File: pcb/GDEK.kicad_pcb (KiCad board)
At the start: 2 copper layers, 133 x 103.5 mm, 101 parts, among them J1 TYPE-C-31-M-13C, J2 AudioJack4, SW1 SK6812MINI, SW10 SK6812MINI, SW11 SK6812MINI, SW12 SK6812MINI, SW13 SK6812MINI, SW14 SK6812MINI, SW15 SK6812MINI, SW16 SK6812MINI, SW17 SK6812MINI, SW18 SK6812MINI, SW19 SK6812MINI, SW2 SK6812MINI, SW20 SK6812MINI, SW21 SK6812MINI, SW22 SK6812MINI, SW23 SK6812MINI, SW24 SK6812MINI, SW25 SK6812MINI, SW26 SK6812MINI, SW27 SK6812MINI, SW28 SK6812MINI, SW29 SK6812MINI, SW3 SK6812MINI, SW30 SK6812MINI, SW31 RotaryEncoder_Switch, SW4 SK6812MINI, SW5 SK6812MINI, SW6 SK6812MINI, SW7 SK6812MINI, SW8 SK6812MINI, SW9 SK6812MINI, U1 RP2040, U2 W25Q128JVS, U3 74AHCT1G125, U4 USBLC6-2P6, U5 XC6210B332MR, Y1 ABM8-272-T3

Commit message: ♻️ Replace LED and reroute them
They are flipped on odd rows to have a better layout not requiring any layer switch because of the new LED footprint with mouse ears.
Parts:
- added C17: 100nF, Capacitor_SMD:C_0402_1005Metric, B.Cu at (137.5, 43.5)
- added C18: 100nF, Capacitor_SMD:C_0402_1005Metric, B.Cu at (24.2, 43.8)
- added C19: 100nF, Capacitor_SMD:C_0402_1005Metric, B.Cu at (-6.95, 22.3)
- added C20: 100nF, Capacitor_SMD:C_0402_1005Metric, B.Cu at (-6.95, 24.3)
- added C21: 100nF, Capacitor_SMD:C_0402_1005Metric, B.Cu at (-6.95, 26.2)
- added C22: 100nF, Capacitor_SMD:C_0402_1005Metric, B.Cu at (-6.95, 28.2)
- added C23: 100nF, Capacitor_SMD:C_0402_1005Metric, B.Cu at (-6.95, 30.2)
- added C24: 100nF, Capacitor_SMD:C_0402_1005Metric, B.Cu at (-6.95, 32.2)
- added C25: 100nF, Capacitor_SMD:C_0402_1005Metric, B.Cu at (-6.95, 34.1)
- added C26: 100nF, Capacitor_SMD:C_0402_1005Metric, B.Cu at (-6.95, 36.1)
- added C27: 100nF, Capacitor_SMD:C_0402_1005Metric, B.Cu at (-6.95, 38.1)
- added C28: 100nF, Capacitor_SMD:C_0402_1005Metric, B.Cu at (-6.95, 40.0)
- added C29: 100nF, Capacitor_SMD:C_0402_1005Metric, B.Cu at (-6.95, 42.0)
- added C30: 100nF, Capacitor_SMD:C_0402_1005Metric, B.Cu at (-9.82, 22.3)
- added C31: 100nF, Capacitor_SMD:C_0402_1005Metric, B.Cu at (-9.82, 24.3)
- added C32: 100nF, Capacitor_SMD:C_0402_1005Metric, B.Cu at (-9.82, 26.2)
- added C33: 100nF, Capacitor_SMD:C_0402_1005Metric, B.Cu at (-9.82, 28.2)
- added C34: 100nF, Capacitor_SMD:C_0402_1005Metric, B.Cu at (-9.82, 30.2)
- added C35: 100nF, Capacitor_SMD:C_0402_1005Metric, B.Cu at (-9.82, 32.2)
- added C36: 100nF, Capacitor_SMD:C_0402_1005Metric, B.Cu at (-9.82, 34.1)
- added C37: 100nF, Capacitor_SMD:C_0402_1005Metric, B.Cu at (-9.82, 36.1)
- added C38: 100nF, Capacitor_SMD:C_0402_1005Metric, B.Cu at (-9.82, 38.1)
- added C39: 100nF, Capacitor_SMD:C_0402_1005Metric, B.Cu at (-9.82, 40.0)
- added C40: 100nF, Capacitor_SMD:C_0402_1005Metric, B.Cu at (-9.82, 42.0)
- added C41: 100nF, Capacitor_SMD:C_0402_1005Metric, B.Cu at (-12.7, 22.3)
- added C42: 100nF, Capacitor_SMD:C_0402_1005Metric, B.Cu at (-12.7, 24.3)
- added C43: 100nF, Capacitor_SMD:C_0402_1005Metric, B.Cu at (-12.7, 26.2)
- added C44: 100nF, Capacitor_SMD:C_0402_1005Metric, B.Cu at (-12.7, 28.2)
- added C45: 100nF, Capacitor_SMD:C_0402_1005Metric, B.Cu at (-12.7, 30.2)
- added C46: 100nF, Capacitor_SMD:C_0402_1005Metric, B.Cu at (-12.7, 32.2)
- added C47: 100nF, Capacitor_SMD:C_0402_1005Metric, B.Cu at (-12.7, 34.1)
- added LD1: SK6812, GDEK:SK6812MINIE, B.Cu at (29.5, 43.8)
- added LD10: SK6812, GDEK:SK6812MINIE, B.Cu at (86.5, 48.2)
- added LD11: SK6812, GDEK:SK6812MINIE, B.Cu at (105.5, 51.8)
- added LD12: SK6812, GDEK:SK6812MINIE, B.Cu at (124.5, 54.2)
- added LD13: SK6812, GDEK:SK6812MINIE, B.Cu at (29.5, 81.8)
- added LD14: SK6812, GDEK:SK6812MINIE, B.Cu at (48.5, 81.8)
- added LD15: SK6812, GDEK:SK6812MINIE, B.Cu at (67.5, 70.8)
- added LD16: SK6812, GDEK:SK6812MINIE, B.Cu at (86.5, 67.2)
- added LD17: SK6812, GDEK:SK6812MINIE, B.Cu at (105.5, 70.8)
- added LD18: SK6812, GDEK:SK6812MINIE, B.Cu at (124.5, 73.2)
- added LD19: SK6812, GDEK:SK6812MINIE, B.Cu at (29.5, 100.8)
- added LD2: SK6812, GDEK:SK6812MINIE, B.Cu at (48.5, 43.8)
- added LD20: SK6812, GDEK:SK6812MINIE, B.Cu at (48.5, 100.8)
- added LD21: SK6812, GDEK:SK6812MINIE, B.Cu at (67.5, 89.8)
- added LD22: SK6812, GDEK:SK6812MINIE, B.Cu at (86.5, 86.2)
- added LD23: SK6812, GDEK:SK6812MINIE, B.Cu at (105.5, 89.8)
- added LD24: SK6812, GDEK:SK6812MINIE, B.Cu at (124.5, 92.2)
- added LD25: SK6812, GDEK:SK6812MINIE, B.Cu at (67.5, 108.8)
- added LD26: SK6812, GDEK:SK6812MINIE, B.Cu at (86.5, 105.2)
- added LD27: SK6812, GDEK:SK6812MINIE, B.Cu at (105.5, 108.8)
- added LD28: SK6812, GDEK:SK6812MINIE, B.Cu at (124.5, 111.2)
- added LD29: SK6812, GDEK:SK6812MINIE, B.Cu at (143.5, 113.8)
- added LD3: SK6812, GDEK:SK6812MINIE, B.Cu at (67.5, 32.8)
- added LD30: SK6812, GDEK:SK6812MINIE, B.Cu at (143.5, 94.8)
- added LD4: SK6812, GDEK:SK6812MINIE, B.Cu at (86.5, 29.2)
- added LD5: SK6812, GDEK:SK6812MINIE, B.Cu at (105.5, 32.8)
- added LD6: SK6812, GDEK:SK6812MINIE, B.Cu at (124.5, 35.2)
- added LD7: SK6812, GDEK:SK6812MINIE, B.Cu at (29.5, 62.8)
- added LD8: SK6812, GDEK:SK6812MINIE, B.Cu at (48.5, 62.8)
- added LD9: SK6812, GDEK:SK6812MINIE, B.Cu at (67.5, 51.8)
- SW1, SW10, SW11, SW12, SW13, SW14, SW15, SW16, SW17, SW18, SW19, SW2, SW20, SW21, SW22, SW23, SW24, SW25, SW26, SW27, SW28, SW29, SW3, SW30, SW4, SW5, SW6, SW7, SW8, SW9: value SK6812MINI -> SW_Push_45deg; footprint GDEK:MX+KailhChoc+GateronKS+SK6812MINI-E_Tight -> GDEK:MX+KailhChoc+GateronKS_Tight
- U2: footprint Package_SO:SOIC-8_5.23x5.23mm_P1.27mm -> Package_SO:SOIC-8_5.3x5.3mm_P1.27mm
- moved R8 1.24 mm to (137.5, 41.3)
- renumbered R to TP1, B to TP2
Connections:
- SW1 pad 1: GND -> /COL0
- SW1 pad 2: Net-(SW1B-DIN) -> Net-(D1-A)
- SW10 pad 1: GND -> /COL3
- SW10 pad 2: Net-(SW10B-DIN) -> Net-(D10-A)
- SW11 pad 1: GND -> /COL4
- SW11 pad 2: Net-(SW10B-DOUT) -> Net-(D11-A)
- SW12 pad 1: GND -> /COL5
- SW12 pad 2: Net-(SW11B-DOUT) -> Net-(D12-A)
- SW13 pad 1: GND -> /COL0
- SW13 pad 2: Net-(SW13B-DIN) -> Net-(D13-A)
- SW14 pad 1: GND -> /COL1
- SW14 pad 2: Net-(SW14B-DIN) -> Net-(D14-A)
- SW15 pad 1: GND -> /COL2
- SW15 pad 2: Net-(SW15B-DIN) -> Net-(D15-A)
- SW16 pad 1: GND -> /COL3
- SW16 pad 2: Net-(SW16B-DIN) -> Net-(D16-A)
- SW17 pad 1: GND -> /COL4
- SW17 pad 2: Net-(SW17B-DIN) -> Net-(D17-A)
- SW18 pad 1: GND -> /COL5
- SW18 pad 2: Net-(SW12B-DOUT) -> Net-(D18-A)
- SW19 pad 1: GND -> /COL0
- SW19 pad 2: Net-(SW13B-DOUT) -> Net-(D19-A)
- SW2 pad 1: GND -> /COL1
- SW2 pad 2: Net-(SW2B-DIN) -> Net-(D2-A)
- SW20 pad 1: GND -> /COL1
- SW20 pad 2: Net-(SW19B-DOUT) -> Net-(D20-A)
- SW21 pad 1: GND -> /COL2
- SW21 pad 2: Net-(SW20B-DOUT) -> Net-(D21-A)
- SW22 pad 1: GND -> /COL3
- SW22 pad 2: Net-(SW21B-DOUT) -> Net-(D22-A)
- SW23 pad 1: GND -> /COL4
- SW23 pad 2: Net-(SW22B-DOUT) -> Net-(D23-A)
- SW24 pad 1: GND -> /COL5
- SW24 pad 2: Net-(SW23B-DOUT) -> Net-(D24-A)
- SW25 pad 1: GND -> /COL0
- SW25 pad 2: Net-(SW25B-DIN) -> Net-(D25-A)
- SW26 pad 1: GND -> /COL1
- SW26 pad 2: Net-(SW26B-DIN) -> Net-(D26-A)
- SW27 pad 1: GND -> /COL2
- SW27 pad 2: Net-(SW27B-DIN) -> Net-(D27-A)
- SW28 pad 1: GND -> /COL3
- SW28 pad 2: Net-(SW28B-DIN) -> Net-(D28-A)
- SW29 pad 1: GND -> /COL4
- SW29 pad 2: Net-(SW29B-DIN) -> Net-(D29-A)
- SW3 pad 1: GND -> /COL2
- SW3 pad 2: Net-(SW3B-DIN) -> Net-(D3-A)
- SW30 pad 1: GND -> /COL5
- SW30 pad 2: Net-(SW24B-DOUT) -> Net-(D30-A)
- SW4 pad 1: GND -> /COL3
- SW4 pad 2: Net-(SW4B-DIN) -> Net-(D4-A)
- SW5 pad 1: GND -> /COL4
- SW5 pad 2: Net-(SW5B-DIN) -> Net-(D5-A)
- SW6 pad 1: GND -> /COL5
- SW6 pad 2: Net-(SW6B-DIN) -> Net-(D6-A)
- SW7 pad 1: GND -> /COL0
- SW7 pad 2: Net-(SW1B-DOUT) -> Net-(D7-A)
- SW8 pad 1: GND -> /COL1
- SW8 pad 2: Net-(SW7B-DOUT) -> Net-(D8-A)
- SW9 pad 1: GND -> /COL2
- SW9 pad 2: Net-(SW8B-DOUT) -> Net-(D9-A)
- U3 pad 4: Net-(SW6B-DIN) -> Net-(LD6-DIN)
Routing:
- net Net-(SW20B-DOUT): track 35.6 -> 0.00 mm
- net Net-(SW8B-DOUT): track 33.5 -> 0.00 mm
- net Net-(SW12B-DOUT): track 31.9 -> 0.00 mm, vias 2 -> 0
- net Net-(SW21B-DOUT): track 28.6 -> 0.00 mm
- net Net-(SW10B-DIN): track 28.6 -> 0.00 mm
- net Net-(SW1B-DOUT): track 28.0 -> 0.00 mm
- net Net-(SW13B-DOUT): track 27.3 -> 0.00 mm
- net Net-(SW19B-DOUT): track 27.1 -> 0.00 mm
- net Net-(SW7B-DOUT): track 27.0 -> 0.00 mm
- net Net-(SW24B-DOUT): track 26.6 -> 0.00 mm, vias 2 -> 0
- net Net-(LD12-DOUT): track 0.00 -> 26.2 mm, vias 0 -> 2
- net Net-(SW23B-DOUT): track 26.1 -> 0.00 mm
- net Net-(SW11B-DOUT): track 26.1 -> 0.00 mm
- net Net-(SW22B-DOUT): track 25.7 -> 0.00 mm
- net Net-(SW10B-DOUT): track 25.7 -> 0.00 mm
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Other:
- board size 133 x 103.5 mm -> 267 x 103.5 mm
- board text added: "v0.1.0"
- board text removed: "v1.0.0"

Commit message: ✨ Update lots of stuff (and make the thumb cluster round)
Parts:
- added C101: 10µF, Capacitor_SMD:C_0402_1005Metric, F.Cu at (246.8, 133.4)
- added C102: 10µF, Capacitor_SMD:C_0402_1005Metric, F.Cu at (246.8, 135.4)
- added C103: 15pF, Capacitor_SMD:C_0402_1005Metric, F.Cu at (246.8, 137.4)
- added C104: 15pF, Capacitor_SMD:C_0402_1005Metric, F.Cu at (246.8, 139.3)
- added C105: 1µF, Capacitor_SMD:C_0402_1005Metric, F.Cu at (246.8, 141.3)
- added C106: 100nF, Capacitor_SMD:C_0402_1005Metric, F.Cu at (246.8, 143.3)
- added C107: 100nF, Capacitor_SMD:C_0402_1005Metric, F.Cu at (246.8, 145.2)
- added C108: 1µF, Capacitor_SMD:C_0402_1005Metric, F.Cu at (246.8, 147.2)
- added C109: 100nF, Capacitor_SMD:C_0402_1005Metric, F.Cu at (246.8, 149.2)
- added C110: 100nF, Capacitor_SMD:C_0402_1005Metric, F.Cu at (246.8, 151.2)
- added C111: 100nF, Capacitor_SMD:C_0402_1005Metric, F.Cu at (249.6, 133.4)
- added C112: 100nF, Capacitor_SMD:C_0402_1005Metric, F.Cu at (249.6, 135.4)
- added C113: 100nF, Capacitor_SMD:C_0402_1005Metric, F.Cu at (249.6, 137.4)
- added C114: 100nF, Capacitor_SMD:C_0402_1005Metric, F.Cu at (249.6, 139.3)
- added C115: 100nF, Capacitor_SMD:C_0402_1005Metric, F.Cu at (249.6, 141.3)
- added C116: 100nF, Capacitor_SMD:C_0402_1005Metric, F.Cu at (249.6, 143.3)
- added C117: 100nF, Capacitor_SMD:C_0402_1005Metric, F.Cu at (249.6, 145.2)
- added C118: 100nF, Capacitor_SMD:C_0402_1005Metric, F.Cu at (249.6, 147.2)
- added C119: 100nF, Capacitor_SMD:C_0402_1005Metric, F.Cu at (249.6, 149.2)
- added C120: 100nF, Capacitor_SMD:C_0402_1005Metric, F.Cu at (249.6, 151.2)
- added C121: 100nF, Capacitor_SMD:C_0402_1005Metric, F.Cu at (252.5, 133.4)
- added C122: 100nF, Capacitor_SMD:C_0402_1005Metric, F.Cu at (252.5, 135.4)
- added C123: 100nF, Capacitor_SMD:C_0402_1005Metric, F.Cu at (252.5, 137.4)
- added C124: 100nF, Capacitor_SMD:C_0402_1005Metric, F.Cu at (252.5, 139.3)
- added C125: 100nF, Capacitor_SMD:C_0402_1005Metric, F.Cu at (252.5, 141.3)
- added C126: 100nF, Capacitor_SMD:C_0402_1005Metric, F.Cu at (252.5, 143.3)
- added C127: 100nF, Capacitor_SMD:C_0402_1005Metric, F.Cu at (252.5, 145.2)
- added C128: 100nF, Capacitor_SMD:C_0402_1005Metric, F.Cu at (252.5, 147.2)
- added C129: 100nF, Capacitor_SMD:C_0402_1005Metric, F.Cu at (252.5, 149.2)
- added C130: 100nF, Capacitor_SMD:C_0402_1005Metric, F.Cu at (252.5, 151.2)
- added C131: 100nF, Capacitor_SMD:C_0402_1005Metric, F.Cu at (255.4, 133.4)
- added C132: 100nF, Capacitor_SMD:C_0402_1005Metric, F.Cu at (255.4, 135.4)
- added C133: 100nF, Capacitor_SMD:C_0402_1005Metric, F.Cu at (255.4, 137.4)
- added C134: 100nF, Capacitor_SMD:C_0402_1005Metric, F.Cu at (255.4, 139.3)
- added C135: 100nF, Capacitor_SMD:C_0402_1005Metric, F.Cu at (255.4, 141.3)
- added C136: 100nF, Capacitor_SMD:C_0402_1005Metric, F.Cu at (255.4, 143.3)
- added C137: 100nF, Capacitor_SMD:C_0402_1005Metric, F.Cu at (255.4, 145.2)
- added C138: 100nF, Capacitor_SMD:C_0402_1005Metric, F.Cu at (255.4, 147.2)
- added C139: 100nF, Capacitor_SMD:C_0402_1005Metric, F.Cu at (255.4, 149.2)
- added C140: 100nF, Capacitor_SMD:C_0402_1005Metric, F.Cu at (255.4, 151.2)
- added C141: 100nF, Capacitor_SMD:C_0402_1005Metric, F.Cu at (258.2, 133.4)
- added C142: 100nF, Capacitor_SMD:C_0402_1005Metric, F.Cu at (258.2, 135.4)
- added C143: 100nF, Capacitor_SMD:C_0402_1005Metric, F.Cu at (258.2, 137.4)
- added C144: 100nF, Capacitor_SMD:C_0402_1005Metric, F.Cu at (258.2, 139.3)
- added C145: 100nF, Capacitor_SMD:C_0402_1005Metric, F.Cu at (258.2, 141.3)
- added C146: 100nF, Capacitor_SMD:C_0402_1005Metric, F.Cu at (258.2, 143.3)
- added C147: 100nF, Capacitor_SMD:C_0402_1005Metric, F.Cu at (258.2, 145.2)
- added D101: D_Small, Diode_SMD:D_SOD-123, F.Cu at (248.2, 107.3)
- added D102: D_Small, Diode_SMD:D_SOD-123, F.Cu at (248.2, 110.7)
- added D103: D_Small, Diode_SMD:D_SOD-123, F.Cu at (248.2, 114.0)
- added D104: D_Small, Diode_SMD:D_SOD-123, F.Cu at (248.2, 117.4)
- added D105: D_Small, Diode_SMD:D_SOD-123, F.Cu at (248.2, 120.7)
- added D106: D_Small, Diode_SMD:D_SOD-123, F.Cu at (248.2, 124.1)
- added D107: D_Small, Diode_SMD:D_SOD-123, F.Cu at (248.2, 127.4)
- added D108: D_Small, Diode_SMD:D_SOD-123, F.Cu at (248.2, 130.8)
- added D109: D_Small, Diode_SMD:D_SOD-123, F.Cu at (254.0, 107.3)
- added D110: D_Small, Diode_SMD:D_SOD-123, F.Cu at (254.0, 110.7)
- added D111: D_Small, Diode_SMD:D_SOD-123, F.Cu at (254.0, 114.0)
- added D112: D_Small, Diode_SMD:D_SOD-123, F.Cu at (254.0, 117.4)
- added D113: D_Small, Diode_SMD:D_SOD-123, F.Cu at (254.0, 120.7)
- added D114: D_Small, Diode_SMD:D_SOD-123, F.Cu at (254.0, 124.1)
- added D115: D_Small, Diode_SMD:D_SOD-123, F.Cu at (254.0, 127.4)
- added D116: D_Small, Diode_SMD:D_SOD-123, F.Cu at (254.0, 130.8)
- added D117: D_Small, Diode_SMD:D_SOD-123, F.Cu at (259.8, 107.3)
- added D118: D_Small, Diode_SMD:D_SOD-123, F.Cu at (259.8, 110.7)
- added D119: D_Small, Diode_SMD:D_SOD-123, F.Cu at (259.8, 114.0)
- added D120: D_Small, Diode_SMD:D_SOD-123, F.Cu at (259.8, 117.4)
- added D121: D_Small, Diode_SMD:D_SOD-123, F.Cu at (259.8, 120.7)
- added D122: D_Small, Diode_SMD:D_SOD-123, F.Cu at (259.8, 124.1)
- added D123: D_Small, Diode_SMD:D_SOD-123, F.Cu at (259.8, 127.4)
- added D124: D_Small, Diode_SMD:D_SOD-123, F.Cu at (259.8, 130.8)
- added D125: D_Small, Diode_SMD:D_SOD-123, F.Cu at (265.6, 107.3)
- added D126: D_Small, Diode_SMD:D_SOD-123, F.Cu at (265.6, 110.7)
- added D127: D_Small, Diode_SMD:D_SOD-123, F.Cu at (265.6, 114.0)
- added D128: D_Small, Diode_SMD:D_SOD-123, F.Cu at (265.6, 117.4)
- added D129: D_Small, Diode_SMD:D_SOD-123, F.Cu at (265.6, 120.7)
- added D130: D_Small, Diode_SMD:D_SOD-123, F.Cu at (265.6, 124.1)
- added D161: B5817, Diode_SMD:D_SOD-323, F.Cu at (288.3, 138.5)
- added D162: PESD3V3L1BA, Diode_SMD:D_SOD-323, F.Cu at (288.3, 141.5)
- added F101: Polyfuse, Fuse:Fuse_0603_1608Metric, F.Cu at (301.4, 129.0)
- added J101: TYPE-C-31-M-13C, GDEK:USB_C_Receptacle_HRO_TYPE-C-31-M-13B, F.Cu at (275.1, 130.3)
- added J102: AudioJack4, GDEK:AUDIO-TH_PJ-320A-4P-DIP, F.Cu at (296.9, 109.3)
- added J103: Debug pads, Connector_PinHeader_2.54mm:PinHeader_1x04_P2.54mm_Vertical, F.Cu at (275.5, 133.7)
- added J3: Debug pads, Connector_PinHeader_2.54mm:PinHeader_1x04_P2.54mm_Vertical, F.Cu at (270.8, 133.7)
- added LD101: SK6812, GDEK:SK6812MINIE, F.Cu at (215.6, 154.1)
- added LD102: SK6812, GDEK:SK6812MINIE, F.Cu at (224.1, 108.2)
- added LD103: SK6812, GDEK:SK6812MINIE, F.Cu at (224.1, 113.3)
- added LD104: SK6812, GDEK:SK6812MINIE, F.Cu at (224.1, 118.4)
- added LD105: SK6812, GDEK:SK6812MINIE, F.Cu at (224.1, 123.5)
- added LD106: SK6812, GDEK:SK6812MINIE, F.Cu at (224.1, 128.6)
- added LD107: SK6812, GDEK:SK6812MINIE, F.Cu at (224.1, 133.7)
- added LD108: SK6812, GDEK:SK6812MINIE, F.Cu at (224.1, 138.8)
- added LD109: SK6812, GDEK:SK6812MINIE, F.Cu at (224.1, 143.9)
- added LD110: SK6812, GDEK:SK6812MINIE, F.Cu at (224.1, 149.0)
- added LD111: SK6812, GDEK:SK6812MINIE, F.Cu at (224.1, 154.1)
- added LD112: SK6812, GDEK:SK6812MINIE, F.Cu at (232.6, 108.2)
- added LD113: SK6812, GDEK:SK6812MINIE, F.Cu at (232.6, 113.3)
- added LD114: SK6812, GDEK:SK6812MINIE, F.Cu at (232.6, 118.4)
- added LD115: SK6812, GDEK:SK6812MINIE, F.Cu at (232.6, 123.5)
- added LD116: SK6812, GDEK:SK6812MINIE, F.Cu at (232.6, 128.6)
- added LD117: SK6812, GDEK:SK6812MINIE, F.Cu at (232.6, 133.7)
- added LD118: SK6812, GDEK:SK6812MINIE, F.Cu at (232.6, 138.8)
- added LD119: SK6812, GDEK:SK6812MINIE, F.Cu at (232.6, 143.9)
- added LD120: SK6812, GDEK:SK6812MINIE, F.Cu at (232.6, 149.0)
- added LD121: SK6812, GDEK:SK6812MINIE, F.Cu at (232.6, 154.1)
- added LD122: SK6812, GDEK:SK6812MINIE, F.Cu at (241.1, 108.2)
- added LD123: SK6812, GDEK:SK6812MINIE, F.Cu at (241.1, 113.3)
- added LD124: SK6812, GDEK:SK6812MINIE, F.Cu at (241.1, 118.4)
- added LD125: SK6812, GDEK:SK6812MINIE, F.Cu at (241.1, 123.5)
- added LD126: SK6812, GDEK:SK6812MINIE, F.Cu at (241.1, 128.6)
- added LD127: SK6812, GDEK:SK6812MINIE, F.Cu at (241.1, 133.7)
- added LD128: SK6812, GDEK:SK6812MINIE, F.Cu at (241.1, 138.8)
- added LD129: SK6812, GDEK:SK6812MINIE, F.Cu at (241.1, 143.9)
- added LD130: SK6812, GDEK:SK6812MINIE, F.Cu at (241.1, 149.0)
- added R101: 1k, Resistor_SMD:R_0402_1005Metric, F.Cu at (270.0, 144.6)
- added R102: 5.1k, Resistor_SMD:R_0402_1005Metric, F.Cu at (270.0, 146.6)
- added R103: 1k, Resistor_SMD:R_0402_1005Metric, F.Cu at (270.0, 148.6)
- added R104: 10kΩ, Resistor_SMD:R_0402_1005Metric, F.Cu at (270.0, 150.6)
- added R105: 470, Resistor_SMD:R_0402_1005Metric, F.Cu at (270.0, 152.6)
- added R106: 27, Resistor_SMD:R_0402_1005Metric, F.Cu at (270.0, 154.6)
- added R107: 27, Resistor_SMD:R_0402_1005Metric, F.Cu at (272.9, 144.6)
- added R108: 5.1k, Resistor_SMD:R_0402_1005Metric, F.Cu at (272.9, 146.6)
- added R109: 5.1k, Resistor_SMD:R_0402_1005Metric, F.Cu at (272.9, 148.6)
- added R110: 1k, Resistor_SMD:R_0402_1005Metric, F.Cu at (272.9, 150.6)
- added R111: 470, Resistor_SMD:R_0402_1005Metric, F.Cu at (272.9, 152.6)
- added SW101: SW_Push_45deg, GDEK:MX+KailhChoc+GateronKS_Tight, F.Cu at (204.4, 15.1)
- added SW102: SW_Push_45deg, GDEK:MX+KailhChoc+GateronKS_Tight, F.Cu at (204.4, 35.2)
- added SW103: SW_Push_45deg, GDEK:MX+KailhChoc+GateronKS_Tight, F.Cu at (204.4, 55.3)
- added SW104: SW_Push_45deg, GDEK:MX+KailhChoc+GateronKS_Tight, F.Cu at (204.4, 75.5)
- added SW105: SW_Push_45deg, GDEK:MX+KailhChoc+GateronKS_Tight, F.Cu at (204.4, 95.6)
- added SW106: SW_Push_45deg, GDEK:MX+KailhChoc+GateronKS_Tight, F.Cu at (224.5, 15.1)
- added SW107: SW_Push_45deg, GDEK:MX+KailhChoc+GateronKS_Tight, F.Cu at (224.5, 35.2)
- added SW108: SW_Push_45deg, GDEK:MX+KailhChoc+GateronKS_Tight, F.Cu at (224.5, 55.3)
- added SW109: SW_Push_45deg, GDEK:MX+KailhChoc+GateronKS_Tight, F.Cu at (224.5, 75.5)
- added SW110: SW_Push_45deg, GDEK:MX+KailhChoc+GateronKS_Tight, F.Cu at (224.5, 95.6)
- added SW111: SW_Push_45deg, GDEK:MX+KailhChoc+GateronKS_Tight, F.Cu at (244.6, 15.1)
- added SW112: SW_Push_45deg, GDEK:MX+KailhChoc+GateronKS_Tight, F.Cu at (244.6, 35.2)
- added SW113: SW_Push_45deg, GDEK:MX+KailhChoc+GateronKS_Tight, F.Cu at (244.6, 55.3)
- added SW114: SW_Push_45deg, GDEK:MX+KailhChoc+GateronKS_Tight, F.Cu at (244.6, 75.5)
- added SW115: SW_Push_45deg, GDEK:MX+KailhChoc+GateronKS_Tight, F.Cu at (244.6, 95.6)
- added SW116: SW_Push_45deg, GDEK:MX+KailhChoc+GateronKS_Tight, F.Cu at (264.8, 15.1)
- added SW117: SW_Push_45deg, GDEK:MX+KailhChoc+GateronKS_Tight, F.Cu at (264.8, 35.2)
- added SW118: SW_Push_45deg, GDEK:MX+KailhChoc+GateronKS_Tight, F.Cu at (264.8, 55.3)
- added SW119: SW_Push_45deg, GDEK:MX+KailhChoc+GateronKS_Tight, F.Cu at (264.8, 75.5)
- added SW120: SW_Push_45deg, GDEK:MX+KailhChoc+GateronKS_Tight, F.Cu at (264.8, 95.6)
- added SW121: SW_Push_45deg, GDEK:MX+KailhChoc+GateronKS_Tight, F.Cu at (284.9, 15.1)
- added SW122: SW_Push_45deg, GDEK:MX+KailhChoc+GateronKS_Tight, F.Cu at (284.9, 35.2)
- added SW123: SW_Push_45deg, GDEK:MX+KailhChoc+GateronKS_Tight, F.Cu at (284.9, 55.3)
- added SW124: SW_Push_45deg, GDEK:MX+KailhChoc+GateronKS_Tight, F.Cu at (284.9, 75.5)
- added SW125: SW_Push_45deg, GDEK:MX+KailhChoc+GateronKS_Tight, F.Cu at (284.9, 95.6)
- added SW126: SW_Push_45deg, GDEK:MX+KailhChoc+GateronKS_Tight, F.Cu at (305.0, 15.1)
- added SW127: SW_Push_45deg, GDEK:MX+KailhChoc+GateronKS_Tight, F.Cu at (305.0, 35.2)
- added SW128: SW_Push_45deg, GDEK:MX+KailhChoc+GateronKS_Tight, F.Cu at (305.0, 55.3)
- added SW129: SW_Push_45deg, GDEK:MX+KailhChoc+GateronKS_Tight, F.Cu at (305.0, 75.5)
- added SW130: SW_Push_45deg, GDEK:MX+KailhChoc+GateronKS_Tight, F.Cu at (305.0, 95.6)
- added SW131: RotaryEncoder_Switch, Rotary_Encoder:RotaryEncoder_Alps_EC11E-Switch_Vertical_H20mm, F.Cu at (270.5, 110.8)
- added TP101: Reset pads, Jumper:SolderJumper-2_P1.3mm_Open_RoundedPad1.0x1.5mm, F.Cu at (283.9, 138.8)
- added TP102: Boot pads, Jumper:SolderJumper-2_P1.3mm_Open_RoundedPad1.0x1.5mm, F.Cu at (283.9, 142.4)
- added U101: RP2040, Package_DFN_QFN:QFN-56-1EP_7x7mm_P0.4mm_EP3.2x3.2mm, F.Cu at (286.4, 132.4)
- added U102: W25Q128JVS, Package_SO:SOIC-8_5.3x5.3mm_P1.27mm, F.Cu at (286.9, 124.3)
- added U103: 74AHCT1G125, Package_TO_SOT_SMD:SOT-353_SC-70-5, F.Cu at (293.2, 129.7)
- added U104: USBLC6-2P6, Package_TO_SOT_SMD:SOT-666, F.Cu at (297.3, 129.6)
- added U105: XC6210B332MR, Package_TO_SOT_SMD:SOT-23-5, F.Cu at (284.3, 151.0)
- added Y101: ABM8-272-T3, Crystal:Crystal_SMD_3225-4Pin_3.2x2.5mm, F.Cu at (284.4, 146.4)
- R1, R10: value 1kΩ -> 1k
- R11, R5: value 470Ω -> 470
- R2: value 5.1kΩ -> 5.1k
- R6, R7: value 27Ω -> 27
- moved LD25 77.0 mm to (143.5, 96.8)
- moved LD30 30.0 mm to (142.0, 124.8), turned to 150 degrees
- moved LD26 19.3 mm to (67.5, 108.8)
- moved LD27 19.3 mm to (86.5, 105.2)
- moved LD28 19.1 mm to (105.5, 108.8)
- moved LD29 18.7 mm to (124.8, 114.5), turned to 165 degrees
- moved SW29 11.7 mm to (144.3, 120.6), turned to -30 degrees
- moved J1 9.15 mm to (140.0, 22.0)
- moved SW28 3.62 mm to (126.0, 109.8), turned to -15 degrees
- moved C3 2.00 mm to (139.4, 60.6)
- moved R1 2.00 mm to (138.2, 62.8)
- moved C1 2.00 mm to (146.3, 47.8)
- moved C10 2.00 mm to (141.3, 47.7)
- moved C12 2.00 mm to (145.5, 52.2)
- moved C15 2.00 mm to (145.5, 56.8)
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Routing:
- net /COL2: track 217.9 -> 251.9 mm
- net Net-(LD29-DIN): track 23.5 -> 0.00 mm
- net /COL4: track 176.0 -> 157.2 mm
- net /COL3: track 203.3 -> 185.7 mm
- net Net-(LD25-DIN): track 14.3 -> 0.00 mm
- net Net-(LD13-DOUT): track 25.5 -> 39.6 mm
- net Net-(D29-A): track 9.81 -> 23.5 mm
- net Net-(LD22-DOUT): track 15.6 -> 4.85 mm
- net +5V: track 21.4 -> 31.9 mm
- net Net-(LD23-DOUT): track 15.2 -> 8.53 mm, vias 0 -> 2
- net unconnected-(LD25-DOUT-Pad4): track 0.00 -> 6.16 mm
- net Net-(LD24-DOUT): track 15.1 -> 10.3 mm, vias 2 -> 0
- net Net-(LD28-DIN): track 15.2 -> 19.8 mm
- net Net-(LD19-DOUT): track 14.1 -> 17.4 mm
- net Net-(LD20-DOUT): track 17.4 -> 14.3 mm
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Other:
- board size 267 x 103.5 mm -> 137.1 x 118.4 mm

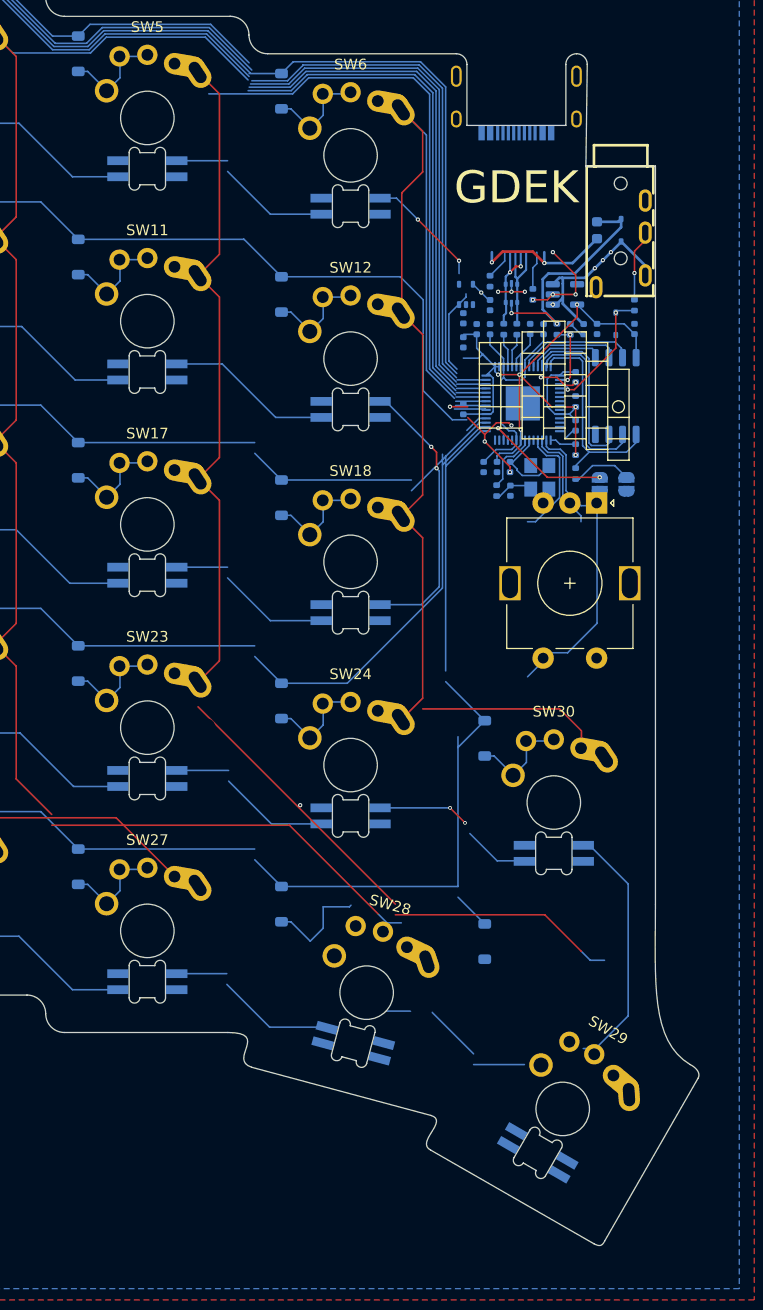
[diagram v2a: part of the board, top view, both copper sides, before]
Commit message: ✨ Finish board outline
Fix thumb cluster’s rounded corners. Add rounded corners near connectors. Add milled slots for USB-C connector’s corners.
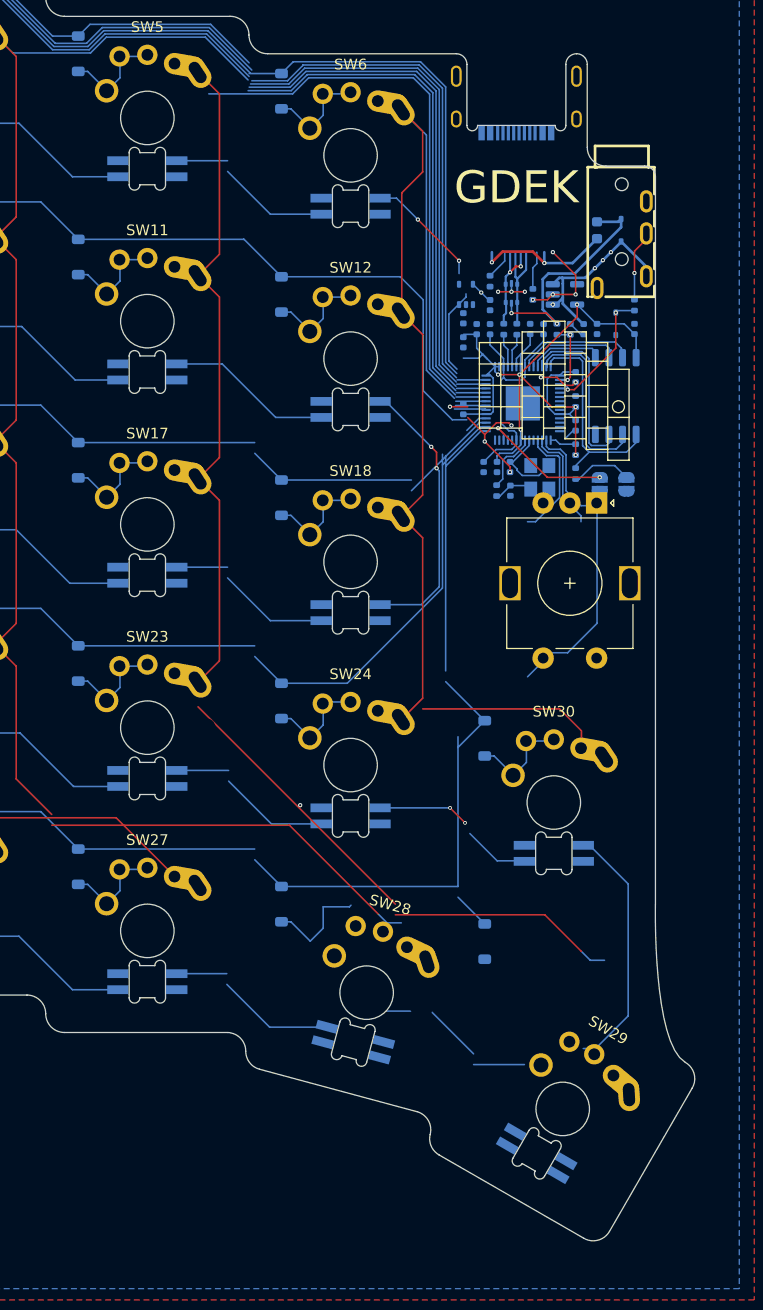
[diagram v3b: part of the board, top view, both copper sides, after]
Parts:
- moved J2 0.12 mm to (149.8, 39.9)
- moved LD30 0.11 mm to (141.9, 124.8)
- moved LD29 0.10 mm to (124.8, 114.4)
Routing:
- net /LED: track 10.7 -> 2.72 mm
- net GND: track 31.9 -> 39.9 mm
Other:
- board size 137.1 x 118.4 mm -> 136.7 x 118 mm

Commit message: ✨ Route LED power and decoupling
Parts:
- removed C101, C102: 10µF, Capacitor_SMD:C_0402_1005Metric
- removed C103, C104: 15pF, Capacitor_SMD:C_0402_1005Metric
- removed C105, C108: 1µF, Capacitor_SMD:C_0402_1005Metric
- removed C106, C107, C109, C110, C111, C112, C113, C114, C115, C116, C117, C118, C119, C120, C121, C122, C123, C124, C125, C126, C127, C128, C129, C130, C131, C132, C133, C134, C135, C136, C137, C138, C139, C140, C141, C142, C143, C144, C145, C146, C147: 100nF, Capacitor_SMD:C_0402_1005Metric
- removed D101, D102, D103, D104, D105, D106, D107, D108, D109, D110, D111, D112, D113, D114, D115, D116, D117, D118, D119, D120, D121, D122, D123, D124, D125, D126, D127, D128, D129, D130: D_Small, Diode_SMD:D_SOD-123
- removed D161: B5817, Diode_SMD:D_SOD-323
- removed D162: PESD3V3L1BA, Diode_SMD:D_SOD-323
- removed F101: Polyfuse, Fuse:Fuse_0603_1608Metric
- removed J101: TYPE-C-31-M-13C, GDEK:USB_C_Receptacle_HRO_TYPE-C-31-M-13B
- removed J102: AudioJack4, GDEK:AUDIO-TH_PJ-320A-4P-DIP
- removed J103, J3: Debug pads, Connector_PinHeader_2.54mm:PinHeader_1x04_P2.54mm_Vertical
- removed LD101, LD102, LD103, LD104, LD105, LD106, LD107, LD108, LD109, LD110, LD111, LD112, LD113, LD114, LD115, LD116, LD117, LD118, LD119, LD120, LD121, LD122, LD123, LD124, LD125, LD126, LD127, LD128, LD129, LD130: SK6812, GDEK:SK6812MINIE
- removed R101, R103, R110: 1k, Resistor_SMD:R_0402_1005Metric
- removed R102, R108, R109: 5.1k, Resistor_SMD:R_0402_1005Metric
- removed R104: 10kΩ, Resistor_SMD:R_0402_1005Metric
- removed R105, R111: 470, Resistor_SMD:R_0402_1005Metric
- removed R106, R107: 27, Resistor_SMD:R_0402_1005Metric
- removed SW101, SW102, SW103, SW104, SW105, SW106, SW107, SW108, SW109, SW110, SW111, SW112, SW113, SW114, SW115, SW116, SW117, SW118, SW119, SW120, SW121, SW122, SW123, SW124, SW125, SW126, SW127, SW128, SW129, SW130: SW_Push_45deg, GDEK:MX+KailhChoc+GateronKS_Tight
- removed SW131: RotaryEncoder_Switch, Rotary_Encoder:RotaryEncoder_Alps_EC11E-Switch_Vertical_H20mm
- removed TP101: Reset pads, Jumper:SolderJumper-2_P1.3mm_Open_RoundedPad1.0x1.5mm
- removed TP102: Boot pads, Jumper:SolderJumper-2_P1.3mm_Open_RoundedPad1.0x1.5mm
- removed U101: RP2040, Package_DFN_QFN:QFN-56-1EP_7x7mm_P0.4mm_EP3.2x3.2mm
- removed U102: W25Q128JVS, Package_SO:SOIC-8_5.3x5.3mm_P1.27mm
- removed U103: 74AHCT1G125, Package_TO_SOT_SMD:SOT-353_SC-70-5
- removed U104: USBLC6-2P6, Package_TO_SOT_SMD:SOT-666
- removed U105: XC6210B332MR, Package_TO_SOT_SMD:SOT-23-5
- removed Y101: ABM8-272-T3, Crystal:Crystal_SMD_3225-4Pin_3.2x2.5mm
- moved C46 174.4 mm to (137.0, 121.8), turned to -90 degrees
- moved C47 173.7 mm to (149.2, 97.0), turned to -90 degrees
- moved C41 159.7 mm to (130.2, 93.5), turned to -90 degrees
- moved C45 155.4 mm to (119.2, 112.3), turned to -90 degrees
- moved C29 137.8 mm to (130.2, 55.5), turned to -90 degrees
- moved C44 137.6 mm to (99.8, 107.5), turned to -90 degrees
- moved C35 134.9 mm to (118.8, 73.0), turned to -90 degrees
- moved C40 130.2 mm to (111.2, 90.0), turned to -90 degrees
- moved C23 125.8 mm to (118.8, 35.0), turned to -90 degrees
- moved C43 121.5 mm to (80.8, 104.0), turned to -90 degrees
- moved C28 118.8 mm to (111.2, 52.0), turned to -90 degrees
- moved C34 116.4 mm to (99.8, 69.5), turned to -90 degrees
- moved C39 112.1 mm to (92.2, 86.5), turned to -90 degrees
- moved C42 111.6 mm to (61.8, 107.5), turned to -90 degrees
- moved C22 106.7 mm to (99.8, 31.5), turned to -90 degrees
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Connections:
- LD25 pad 2: Net-(LD25-DIN) -> Net-(LD24-DOUT)
- LD25 pad 4: unconnected-(LD25-DOUT-Pad4) -> Net-(LD25-DOUT)
- LD26 pad 4: Net-(LD25-DIN) -> unconnected-(LD26-DOUT-Pad4)
- LD30 pad 2: Net-(LD24-DOUT) -> Net-(LD25-DOUT)
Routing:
- net +5V: track 31.9 -> 111.7 mm, vias 6 -> 35
- net Net-(LD25-DOUT): track 0.00 -> 40.4 mm
- net /COL4: track 157.2 -> 191.3 mm, vias 1 -> 0
- net /COL2: track 251.9 -> 219.3 mm
- net Net-(D29-A): track 23.5 -> 0.00 mm
- net /COL3: track 185.7 -> 204.9 mm
- net /ROW3: track 140.3 -> 123.2 mm
- net Net-(LD29-DIN): track 0.00 -> 15.7 mm
- net Net-(LD13-DOUT): track 39.6 -> 25.5 mm
- net Net-(D28-A): track 12.3 -> 0.00 mm
- net Net-(LD22-DOUT): track 4.85 -> 15.6 mm
- net /ROW4: track 128.9 -> 138.0 mm
- net Net-(LD23-DOUT): track 8.53 -> 15.6 mm, vias 2 -> 0
- net unconnected-(LD25-DOUT-Pad4): track 6.16 -> 0.00 mm
- net Net-(LD24-DOUT): track 10.3 -> 15.6 mm, vias 0 -> 2
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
